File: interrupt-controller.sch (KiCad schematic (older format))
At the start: 20 parts

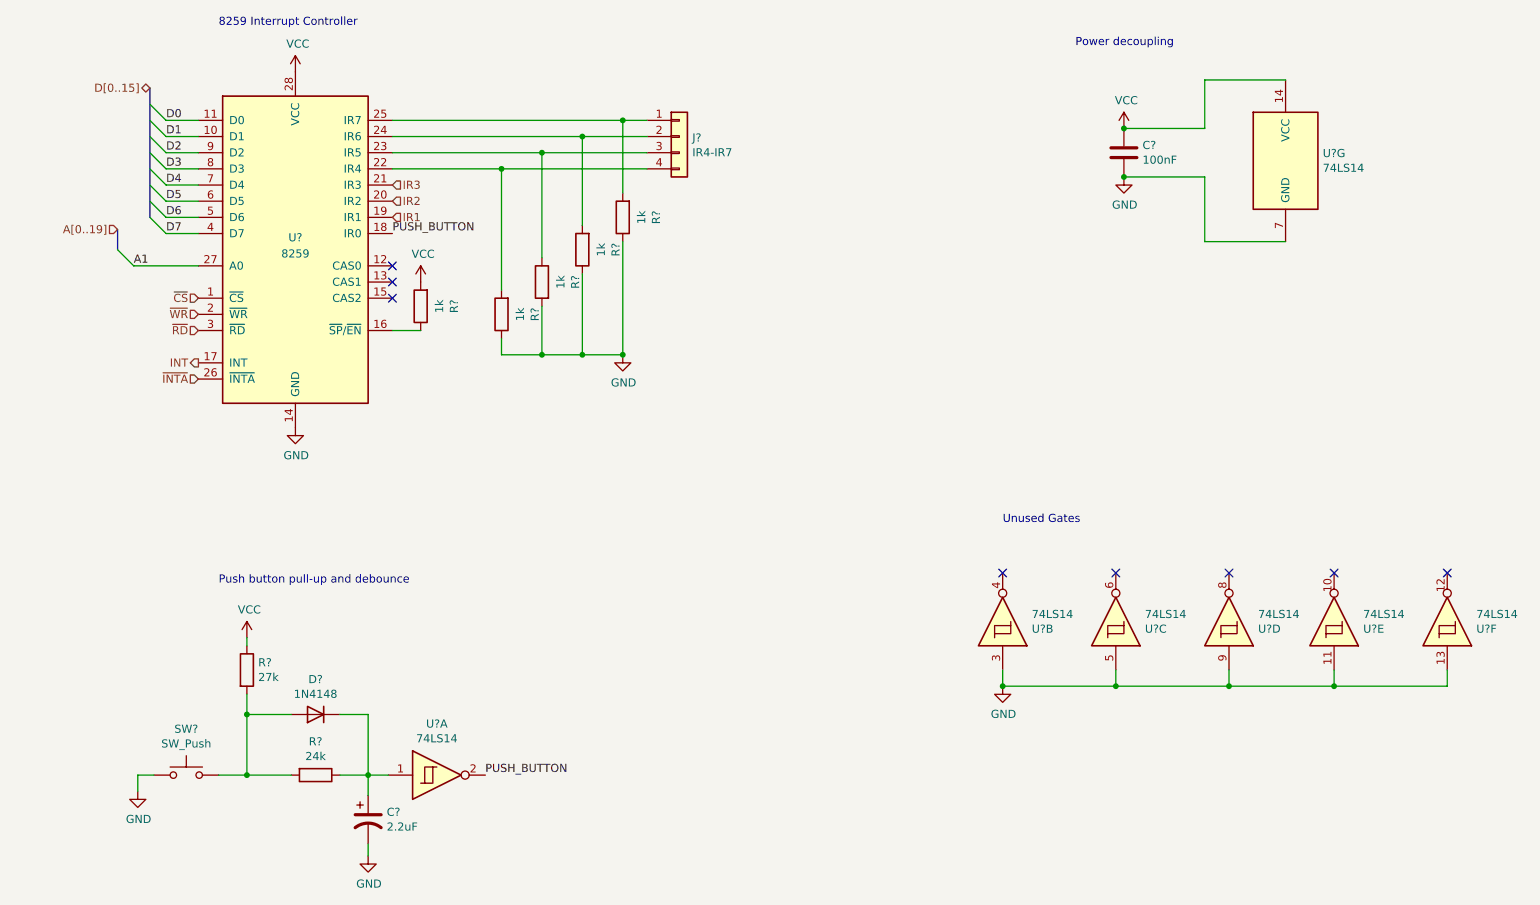
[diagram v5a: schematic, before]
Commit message: Assign footprints for most symbols
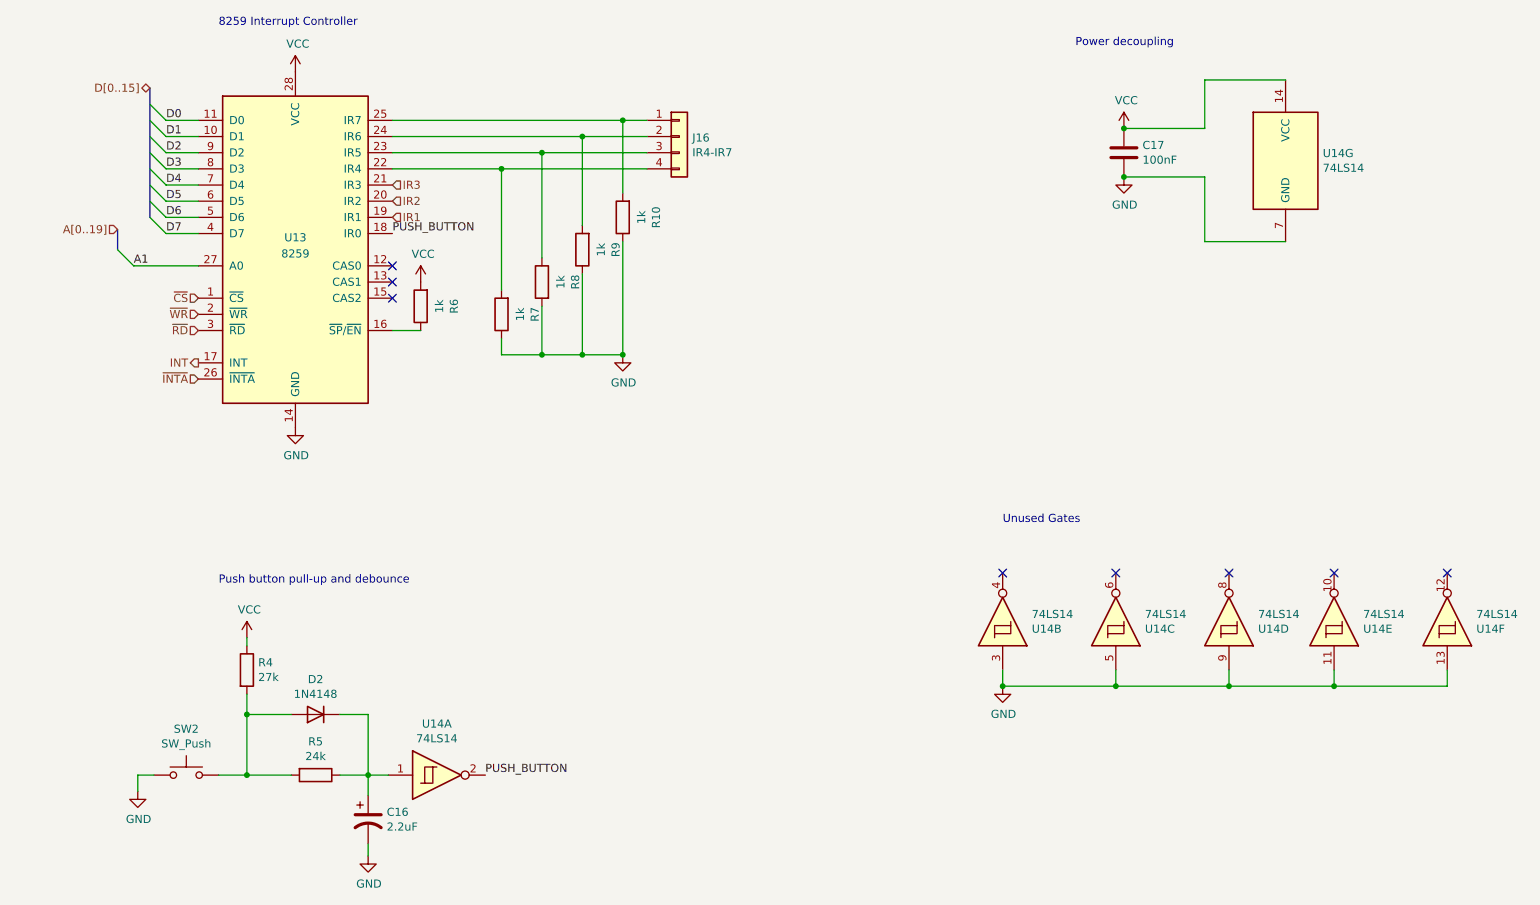
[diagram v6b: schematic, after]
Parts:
- C17: renamed from C?; footprint (none) -> Capacitor_THT:C_Rect_L4.0mm_W2.5mm_P2.50mm
- J16: renamed from J?; footprint (none) -> Connector_PinHeader_2.54mm:PinHeader_1x03_P2.54mm_Vertical
- R10, R4, R5, R6, R7, R8, R9: renamed from R?; footprint (none) -> Resistor_THT:R_Axial_DIN0207_L6.3mm_D2.5mm_P10.16mm_Horizontal
- SW2: renamed from SW?; footprint (none) -> Button_Switch_Keyboard:SW_Cherry_MX_1.00u_PCB
- U14: renamed from U?; footprint (none) -> Package_DIP:DIP-14_W7.62mm
- gave numbers to parts that had none: 3
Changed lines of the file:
@@
 $EndDescr
 $Comp
-L Device:C C?
+L Device:C C17
 U 1 1 61CCFA90
 P 8250 2350
-F 0 "C?" H 8365 2396 50  0000 L CNN
+F 0 "C17" H 8365 2396 50  0000 L CNN
 F 1 "100nF" H 8365 2305 50  0000 L CNN
-F 2 "" H 8288 2200 50  0001 C CNN
+F 2 "Capacitor_THT:C_Rect_L4.0mm_W2.5mm_P2.50mm" H 8288 2200 50  0001 C CNN
 F 3 "~" H 8250 2350 50  0001 C CNN
 	1    8250 2350
@@
 $EndComp
 $Comp
-L power:VCC #PWR?
+L power:VCC #PWR0151
 U 1 1 61CD0125
 P 8250 2200
-F 0 "#PWR?" H 8250 2050 50  0001 C CNN
+F 0 "#PWR0151" H 8250 2050 50  0001 C CNN
 F 1 "VCC" H 8265 2373 50  0000 C CNN
 F 2 "" H 8250 2200 50  0001 C CNN
@@
 $EndComp
 $Comp
-L power:GND #PWR?
+L power:GND #PWR0152
 U 1 1 61CD0589
 P 8250 2500
-F 0 "#PWR?" H 8250 2250 50  0001 C CNN
+F 0 "#PWR0152" H 8250 2250 50  0001 C CNN
 F 1 "GND" H 8255 2327 50  0000 C CNN
 F 2 "" H 8250 2500 50  0001 C CNN
@@
 Power decoupling
 $Comp
-L Device:R R?
+L Device:R R6
 U 1 1 620462B6
 P 3900 3300
-F 0 "R?" V 3693 3300 50  0000 C CNN
+F 0 "R6" V 3693 3300 50  0000 C CNN
 F 1 "1k" V 3784 3300 50  0000 C CNN
-F 2 "" V 3830 3300 50  0001 C CNN
+F 2 "Resistor_THT:R_Axial_DIN0207_L6.3mm_D2.5mm_P10.16mm_Horizontal" V 3830 3300 50  0001 C CNN
 F 3 "~" H 3900 3300 50  0001 C CNN
 	1    3900 3300
@@
 $EndComp
 $Comp
-L power:VCC #PWR?
+L power:VCC #PWR0153
 U 1 1 61CBB753
 P 3900 3150
-F 0 "#PWR?" H 3900 3000 50  0001 C CNN
+F 0 "#PWR0153" H 3900 3000 50  0001 C CNN
 F 1 "VCC" H 3915 3323 50  0000 C CNN
 F 2 "" H 3900 3150 50  0001 C CNN
@@
 NoConn ~ 3725 3050
 $Comp
-L power:GND #PWR?
+L power:GND #PWR0154
 U 1 1 61CBC8B0
 P 3125 4050
-F 0 "#PWR?" H 3125 3800 50  0001 C CNN
+F 0 "#PWR0154" H 3125 3800 50  0001 C CNN
 F 1 "GND" H 3130 3877 50  0000 C CNN
 F 2 "" H 3125 4050 50  0001 C CNN
@@
 $EndComp
 $Comp
-L power:VCC #PWR?
+L power:VCC #PWR0155
 U 1 1 61CBC39E
 P 3125 1850
-F 0 "#PWR?" H 3125 1700 50  0001 C CNN
+F 0 "#PWR0155" H 3125 1700 50  0001 C CNN
 F 1 "VCC" H 3140 2023 50  0000 C CNN
 F 2 "" H 3125 1850 50  0001 C CNN
@@
 $EndComp
 $Comp
-L Interface:8259 U?
+L Interface:8259 U13
 U 1 1 61CB9580
 P 3125 2950
-F 0 "U?" H 3125 3025 50  0000 C CNN
+F 0 "U13" H 3125 3025 50  0000 C CNN
 F 1 "8259" H 3125 2925 50  0000 C CNN
 F 2 "Package_DIP:DIP-28_W15.24mm" H 3125 2950 50  0001 C CIN
@@
 $EndComp
 $Comp
-L Connector_Generic:Conn_01x04 J?
+L Connector_Generic:Conn_01x04 J16
 U 1 1 61CBD97F
 P 5500 2250
-F 0 "J?" H 5580 2242 50  0000 L CNN
+F 0 "J16" H 5580 2242 50  0000 L CNN
 F 1 "IR4-IR7" H 5580 2151 50  0000 L CNN
-F 2 "" H 5500 2250 50  0001 C CNN
+F 2 "Connector_PinHeader_2.54mm:PinHeader_1x03_P2.54mm_Vertical" H 5500 2250 50  0001 C CNN
 F 3 "~" H 5500 2250 50  0001 C CNN
 	1    5500 2250
@@
 $EndComp
 $Comp
-L Device:R R?
+L Device:R R9
 U 1 1 620795B1
 P 4900 2950
-F 0 "R?" V 4693 2950 50  0000 C CNN
+F 0 "R9" V 4693 2950 50  0000 C CNN
 F 1 "1k" V 4784 2950 50  0000 C CNN
-F 2 "" V 4830 2950 50  0001 C CNN
+F 2 "Resistor_THT:R_Axial_DIN0207_L6.3mm_D2.5mm_P10.16mm_Horizontal" V 4830 2950 50  0001 C CNN
 F 3 "~" H 4900 2950 50  0001 C CNN
 	1    4900 2950
@@
 $EndComp
 $Comp
-L Device:R R?
+L Device:R R8
 U 1 1 6207A5B7
 P 4650 3150
-F 0 "R?" V 4443 3150 50  0000 C CNN
+F 0 "R8" V 4443 3150 50  0000 C CNN
 F 1 "1k" V 4534 3150 50  0000 C CNN
-F 2 "" V 4580 3150 50  0001 C CNN
+F 2 "Resistor_THT:R_Axial_DIN0207_L6.3mm_D2.5mm_P10.16mm_Horizontal" V 4580 3150 50  0001 C CNN
 F 3 "~" H 4650 3150 50  0001 C CNN
 	1    4650 3150
@@
 $EndComp
 $Comp
-L Device:R R?
+L Device:R R7
 U 1 1 6207B315
 P 4400 3350
-F 0 "R?" V 4193 3350 50  0000 C CNN
+F 0 "R7" V 4193 3350 50  0000 C CNN
 F 1 "1k" V 4284 3350 50  0000 C CNN
-F 2 "" V 4330 3350 50  0001 C CNN
+F 2 "Resistor_THT:R_Axial_DIN0207_L6.3mm_D2.5mm_P10.16mm_Horizontal" V 4330 3350 50  0001 C CNN
 F 3 "~" H 4400 3350 50  0001 C CNN
 	1    4400 3350
@@
 	3725 3450 3900 3450
 $Comp
-L Device:R R?
+L Device:R R10
 U 1 1 620A9FA3
 P 5150 2750
-F 0 "R?" V 4943 2750 50  0000 C CNN
+F 0 "R10" V 4943 2750 50  0000 C CNN
 F 1 "1k" V 5034 2750 50  0000 C CNN
-F 2 "" V 5080 2750 50  0001 C CNN
+F 2 "Resistor_THT:R_Axial_DIN0207_L6.3mm_D2.5mm_P10.16mm_Horizontal" V 5080 2750 50  0001 C CNN
 F 3 "~" H 5150 2750 50  0001 C CNN
 	1    5150 2750
@@
 $EndComp
 $Comp
-L power:GND #PWR?
+L power:GND #PWR0156
 U 1 1 620B0910
 P 5150 3600
-F 0 "#PWR?" H 5150 3350 50  0001 C CNN
+F 0 "#PWR0156" H 5150 3350 50  0001 C CNN
 F 1 "GND" H 5155 3427 50  0000 C CNN
 F 2 "" H 5150 3600 50  0001 C CNN
@@
 	4400 2450 5300 2450
 $Comp
-L 74xx:74LS14 U?
+L 74xx:74LS14 U14
 U 7 1 6223011F
 P 9250 2400
-F 0 "U?" H 9480 2446 50  0000 L CNN
+F 0 "U14" H 9480 2446 50  0000 L CNN
 F 1 "74LS14" H 9480 2355 50  0000 L CNN
-F 2 "" H 9250 2400 50  0001 C CNN
+F 2 "Package_DIP:DIP-14_W7.62mm" H 9250 2400 50  0001 C CNN
 F 3 "http://www.ti.com/lit/gpn/sn74LS14" H 9250 2400 50  0001 C CNN
 	7    9250 2400
@@
 Connection ~ 8250 2500
 $Comp
-L Switch:SW_Push SW?
+L Switch:SW_Push SW2
 U 1 1 62279DA5
 P 2450 6200
-F 0 "SW?" H 2450 6485 50  0000 C CNN
+F 0 "SW2" H 2450 6485 50  0000 C CNN
 F 1 "SW_Push" H 2450 6394 50  0000 C CNN
-F 2 "" H 2450 6400 50  0001 C CNN
+F 2 "Button_Switch_Keyboard:SW_Cherry_MX_1.00u_PCB" H 2450 6400 50  0001 C CNN
 F 3 "~" H 2450 6400 50  0001 C CNN
 	1    2450 6200
@@
 $EndComp
 $Comp
-L power:GND #PWR?
+L power:GND #PWR0157
 U 1 1 62279DAB
 P 2150 6300
-F 0 "#PWR?" H 2150 6050 50  0001 C CNN
+F 0 "#PWR0157" H 2150 6050 50  0001 C CNN
 F 1 "GND" H 2155 6127 50  0000 C CNN
 F 2 "" H 2150 6300 50  0001 C CNN
@@
 	2150 6200 2250 6200
 $Comp
-L Device:R R?
+L Device:R R4
 U 1 1 62279DB3
 P 2825 5550
-F 0 "R?" H 2895 5596 50  0000 L CNN
+F 0 "R4" H 2895 5596 50  0000 L CNN
 F 1 "27k" H 2895 5505 50  0000 L CNN
-F 2 "" V 2755 5550 50  0001 C CNN
+F 2 "Resistor_THT:R_Axial_DIN0207_L6.3mm_D2.5mm_P10.16mm_Horizontal" V 2755 5550 50  0001 C CNN
 F 3 "~" H 2825 5550 50  0001 C CNN
 	1    2825 5550
@@
 	2825 5400 2825 5350
 $Comp
-L power:VCC #PWR?
+L power:VCC #PWR0158
 U 1 1 62279DBC
 P 2825 5350
-F 0 "#PWR?" H 2825 5200 50  0001 C CNN
+F 0 "#PWR0158" H 2825 5200 50  0001 C CNN
 F 1 "VCC" H 2840 5523 50  0000 C CNN
 F 2 "" H 2825 5350 50  0001 C CNN
@@
 Push button pull-up and debounce
 $Comp
-L Device:R R?
+L Device:R R5
 U 1 1 62279DC5
 P 3250 6200
-F 0 "R?" V 3043 6200 50  0000 C CNN
+F 0 "R5" V 3043 6200 50  0000 C CNN
 F 1 "24k" V 3134 6200 50  0000 C CNN
-F 2 "" V 3180 6200 50  0001 C CNN
+F 2 "Resistor_THT:R_Axial_DIN0207_L6.3mm_D2.5mm_P10.16mm_Horizontal" V 3180 6200 50  0001 C CNN
 F 3 "~" H 3250 6200 50  0001 C CNN
 	1    3250 6200
@@
 $EndComp
 $Comp
-L Diode:1N4148 D?
+L Diode:1N4148 D2
 U 1 1 62279DCB
 P 3250 5825
-F 0 "D?" H 3250 5608 50  0000 C CNN
+F 0 "D2" H 3250 5608 50  0000 C CNN
 F 1 "1N4148" H 3250 5699 50  0000 C CNN
 F 2 "Diode_THT:D_DO-35_SOD27_P7.62mm_Horizontal" H 3250 5650 50  0001 C CNN
@@
 	3575 6200 3575 6325
 $Comp
-L Device:CP1 C?
+L Device:CP1 C16
 U 1 1 62279DD9
 P 3575 6475
-F 0 "C?" H 3690 6521 50  0000 L CNN
+F 0 "C16" H 3690 6521 50  0000 L CNN
 F 1 "2.2uF" H 3690 6430 50  0000 L CNN
 F 2 "" H 3575 6475 50  0001 C CNN
@@
 	3575 6625 3575 6700
 $Comp
-L power:GND #PWR?
+L power:GND #PWR0159
 U 1 1 62279DE0
 P 3575 6700
-F 0 "#PWR?" H 3575 6450 50  0001 C CNN
+F 0 "#PWR0159" H 3575 6450 50  0001 C CNN
 F 1 "GND" H 3580 6527 50  0000 C CNN
 F 2 "" H 3575 6700 50  0001 C CNN
@@
 PUSH_BUTTON
 $Comp
-L 74xx:74LS14 U?
+L 74xx:74LS14 U14
 U 1 1 62279DE8
 P 4000 6200
-F 0 "U?" H 4000 6517 50  0000 C CNN
+F 0 "U14" H 4000 6517 50  0000 C CNN
 F 1 "74LS14" H 4000 6426 50  0000 C CNN
-F 2 "" H 4000 6200 50  0001 C CNN
+F 2 "Package_DIP:DIP-14_W7.62mm" H 4000 6200 50  0001 C CNN
 F 3 "http://www.ti.com/lit/gpn/sn74LS14" H 4000 6200 50  0001 C CNN
 	1    4000 6200
@@
 Unused Gates
 $Comp
-L 74xx:74LS14 U?
+L 74xx:74LS14 U14
 U 2 1 6221FF56
 P 7500 5250
-F 0 "U?" V 7454 5430 50  0000 L CNN
+F 0 "U14" V 7454 5430 50  0000 L CNN
 F 1 "74LS14" V 7545 5430 50  0000 L CNN
-F 2 "" H 7500 5250 50  0001 C CNN
+F 2 "Package_DIP:DIP-14_W7.62mm" H 7500 5250 50  0001 C CNN
 F 3 "http://www.ti.com/lit/gpn/sn74LS14" H 7500 5250 50  0001 C CNN
 	2    7500 5250
@@
 $EndComp
 $Comp
-L 74xx:74LS14 U?
+L 74xx:74LS14 U14
 U 3 1 62228C38
 P 8200 5250
-F 0 "U?" V 8154 5430 50  0000 L CNN
+F 0 "U14" V 8154 5430 50  0000 L CNN
 F 1 "74LS14" V 8245 5430 50  0000 L CNN
-F 2 "" H 8200 5250 50  0001 C CNN
+F 2 "Package_DIP:DIP-14_W7.62mm" H 8200 5250 50  0001 C CNN
 F 3 "http://www.ti.com/lit/gpn/sn74LS14" H 8200 5250 50  0001 C CNN
 	3    8200 5250
@@
 $EndComp
 $Comp
-L 74xx:74LS14 U?
+L 74xx:74LS14 U14
 U 4 1 6222A294
 P 8900 5250
-F 0 "U?" V 8854 5430 50  0000 L CNN
+F 0 "U14" V 8854 5430 50  0000 L CNN
 F 1 "74LS14" V 8945 5430 50  0000 L CNN
-F 2 "" H 8900 5250 50  0001 C CNN
+F 2 "Package_DIP:DIP-14_W7.62mm" H 8900 5250 50  0001 C CNN
 F 3 "http://www.ti.com/lit/gpn/sn74LS14" H 8900 5250 50  0001 C CNN
 	4    8900 5250
@@
 $EndComp
 $Comp
-L 74xx:74LS14 U?
+L 74xx:74LS14 U14
 U 5 1 6222BF93
 P 9550 5250
-F 0 "U?" V 9504 5430 50  0000 L CNN
+F 0 "U14" V 9504 5430 50  0000 L CNN
 F 1 "74LS14" V 9595 5430 50  0000 L CNN
-F 2 "" H 9550 5250 50  0001 C CNN
+F 2 "Package_DIP:DIP-14_W7.62mm" H 9550 5250 50  0001 C CNN
 F 3 "http://www.ti.com/lit/gpn/sn74LS14" H 9550 5250 50  0001 C CNN
 	5    9550 5250
@@
 $EndComp
 $Comp
-L 74xx:74LS14 U?
+L 74xx:74LS14 U14
 U 6 1 6222E721
 P 10250 5250
-F 0 "U?" V 10204 5430 50  0000 L CNN
+F 0 "U14" V 10204 5430 50  0000 L CNN
 F 1 "74LS14" V 10295 5430 50  0000 L CNN
-F 2 "" H 10250 5250 50  0001 C CNN
+F 2 "Package_DIP:DIP-14_W7.62mm" H 10250 5250 50  0001 C CNN
 F 3 "http://www.ti.com/lit/gpn/sn74LS14" H 10250 5250 50  0001 C CNN
 	6    10250 5250
@@
 Connection ~ 8200 5650
 $Comp
-L power:GND #PWR?
+L power:GND #PWR0160
 U 1 1 622CFBD1
 P 7500 5650
-F 0 "#PWR?" H 7500 5400 50  0001 C CNN
+F 0 "#PWR0160" H 7500 5400 50  0001 C CNN
 F 1 "GND" H 7505 5477 50  0000 C CNN
 F 2 "" H 7500 5650 50  0001 C CNN

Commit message: Assigned footprints
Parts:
- C16: footprint (none) -> Capacitor_THT:CP_Radial_D5.0mm_P2.00mm
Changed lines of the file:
@@
 F 0 "C16" H 3690 6521 50  0000 L CNN
 F 1 "2.2uF" H 3690 6430 50  0000 L CNN
-F 2 "" H 3575 6475 50  0001 C CNN
+F 2 "Capacitor_THT:CP_Radial_D5.0mm_P2.00mm" H 3575 6475 50  0001 C CNN
 F 3 "~" H 3575 6475 50  0001 C CNN
 	1    3575 6475
